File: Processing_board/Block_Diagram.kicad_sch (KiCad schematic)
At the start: 0 parts

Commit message: added Block Diagram (in KiCad and PDF) ; minor silkscreen cleanup
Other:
- note added: "16x PIN HEADER"
- note added: "1V8"
- note added: "2x PIN HEADER"
- note added: "3V3"
- note added: "4x PIN HEADER"
- note added: "5V"
- note added: "6x PIN HEADER"
- note added: "ADC"
- note added: "ADS7953"
- note added: "BGS13"
- note added: "BLE (3 DIFFERENT ANTENNA TYPES)"
- note added: "BOOT button"
- note added: "CH0 ... CH15"
- note added: "CONTROLLED IMPEDANCE 50 OHM TRACE"
- note added: "D"
- note added: "D+ D- VBUS"
- note added: "DLF162500LT"
- note added: "G"
- note added: "If PWR = 5V -> bypass 1st LDO with double jumpers PMOS blocks current from PWR when VBUS is on 5V is actually ~4.6V because of Schottky Diodes"
- note added: "LOW-PASS FILTER"
- note added: "MCP-2200"
- note added: "MCU"
- note added: "MXO AINP"
- note added: "OPA192"
- note added: "PMOS"
- note added: "POWER ADAPTATION"
- note added: "PWR"
- note added: "PWR LED"
- note added: "PWR for EMG Modules"
- note added: "REF5025"
- note added: "REFP"
- note added: "RESET button"
- note added: "RF-CAPABLE SWITCH IC"
- note added: "RX LED"
- note added: "S"
- note added: "SCK, MISO, MOSI, *CS"
- note added: "STM32WBA63CIU6"
- note added: "SWCLK SWDI SWD_TRACES NRST 3V3 GND"
- note added: "Status LED"
- note added: "TRACE ANT CHIP ANT EXTERNAL ANT"
- note added: "TX LED"
- note added: "TX RX 3V3 GND"
- note added: "TX, RX"
- note added: "USB-C CONNECTOR"
- note added: "USB-TO-UART IC"
- note added: "VBUS"
- company: N-Pulse -> (none)

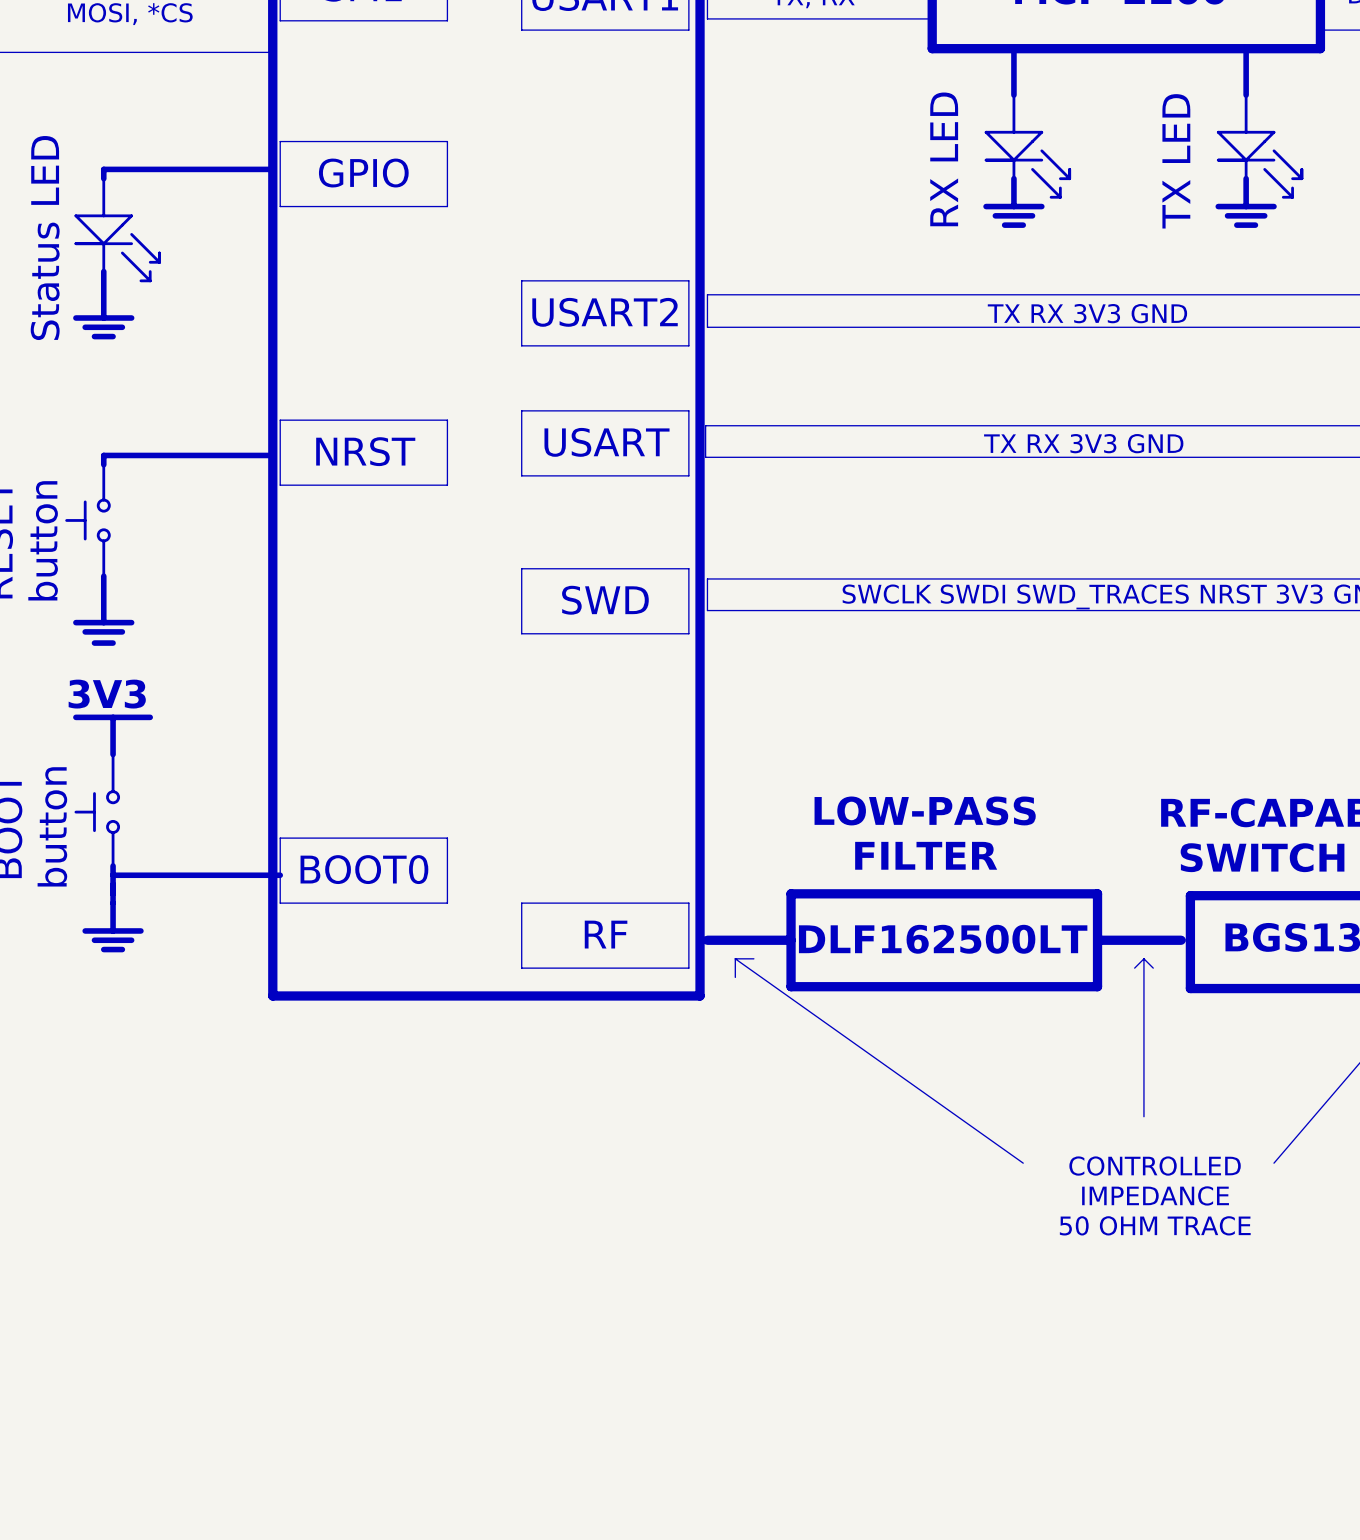
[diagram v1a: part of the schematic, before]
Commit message: UART3 doesn't exist, modified block diagram
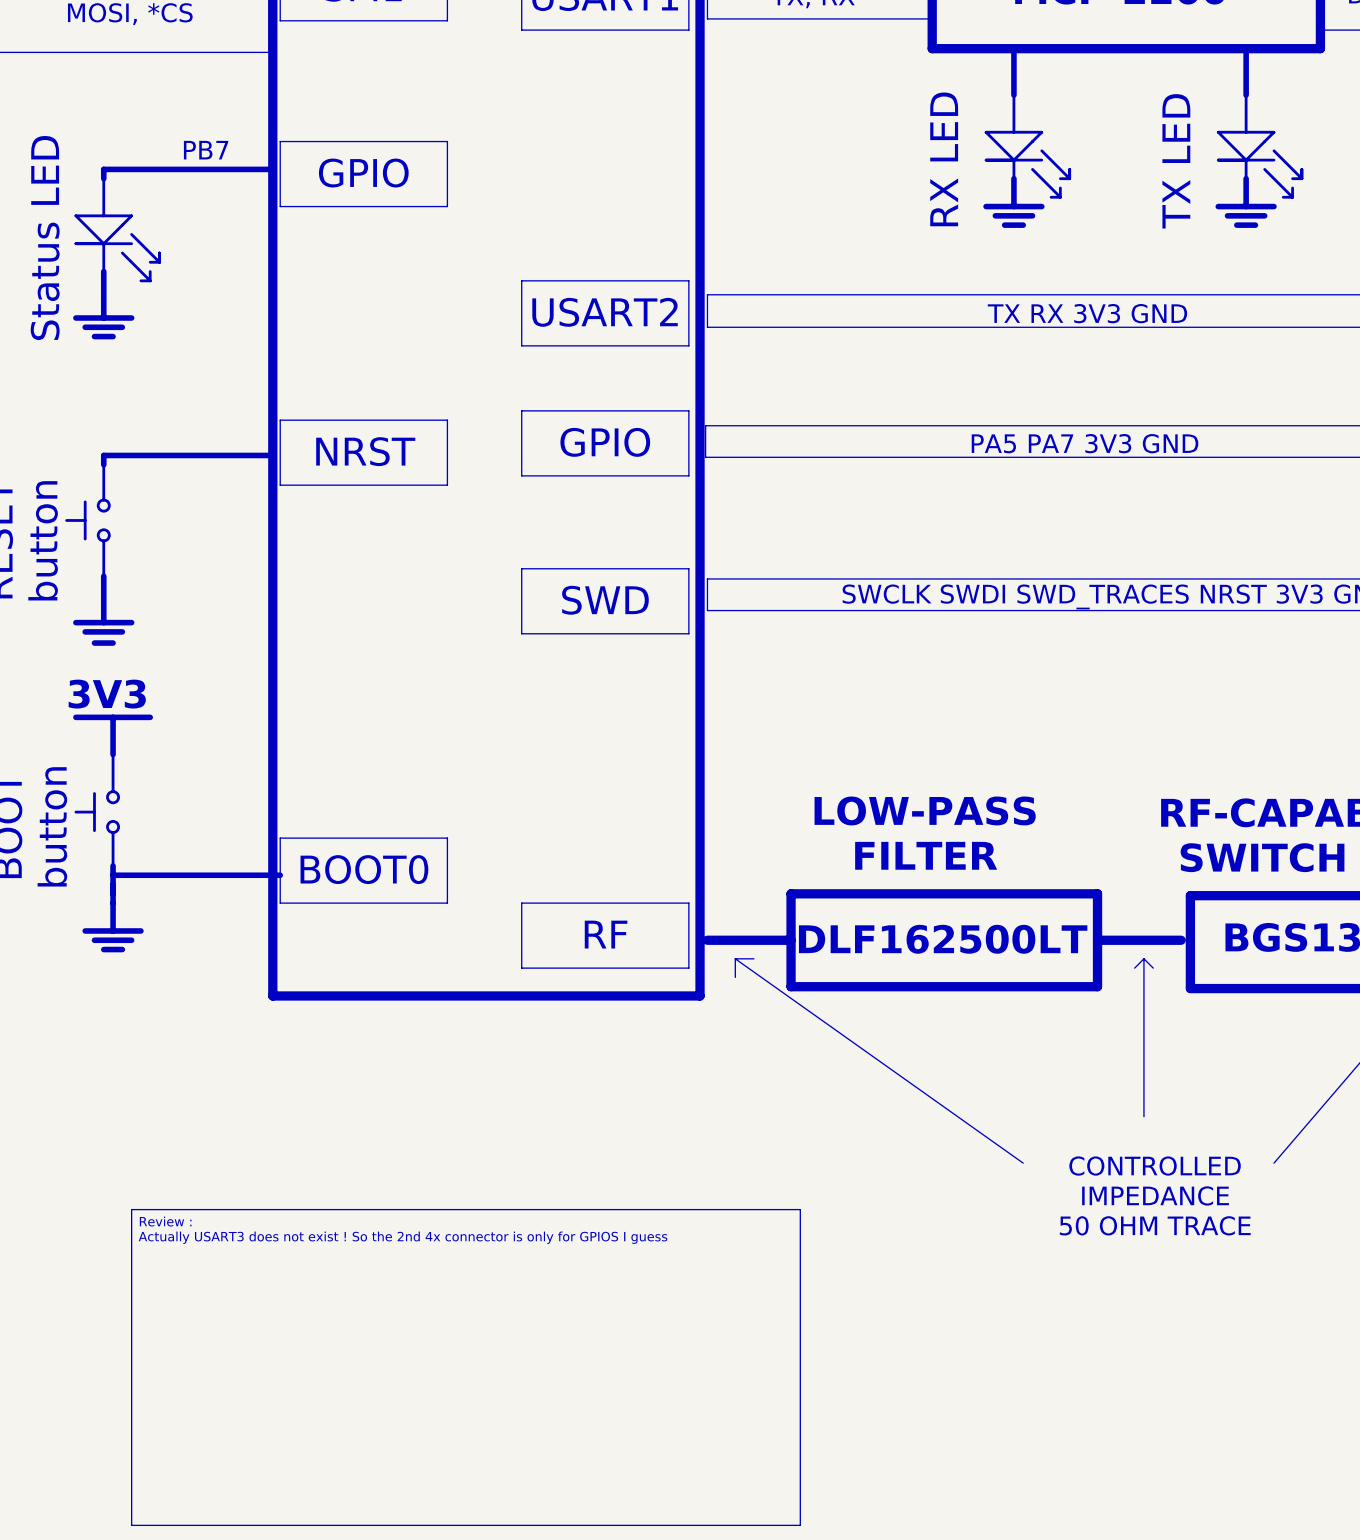
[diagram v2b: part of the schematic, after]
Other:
- note added: "PA5 PA7 3V3 GND"
- note added: "PB7"
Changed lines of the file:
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@@
 			(width 0)
 			(type solid)
-			(color 230 89 209 0.5)
-		)
-		(fill
-			(type color)
-			(color 230 89 209 0.5019607843)
+			(color 145 222 230 0.5)
+		)
+		(fill
+			(type color)
+			(color 145 222 230 0.5)
 		)
 	)
@@
 		)
 	)
-	(text "3V3"
-		(exclude_from_sim no)
-		(at 170.688 139.446 0)
-		(effects
-			(font
-				(size 3.81 3.81)
-				(thickness 0.762)
-				(bold yes)
-				(color 255 30 30 1)
-			)
-		)
-	)
-	(text "4x PIN\nHEADER"
-		(exclude_from_sim no)
-		(at 384.81 86.36 0)
-		(effects
-			(font
-				(size 3.81 3.81)
-				(thickness 0.762)
-				(bold yes)
-				(color 0 0 0 1)
-			)
-		)
-	)
-	(text "CONTROLLED \nIMPEDANCE \n50 OHM TRACE"
-		(exclude_from_sim no)
-		(at 313.944 208.026 0)
+	(text "PB7\n"
+		(exclude_from_sim no)
+		(at 184.15 65.024 0)
 		(effects
 			(font
@@
 		)
 	)
-	(text "USB-C \nCONNECTOR"
-		(exclude_from_sim no)
-		(at 385.826 44.45 0)
+	(text "3V3"
+		(exclude_from_sim no)
+		(at 170.688 139.446 0)
+		(effects
+			(font
+				(size 3.81 3.81)
+				(thickness 0.762)
+				(bold yes)
+				(color 255 30 30 1)
+			)
+		)
+	)
+	(text "4x PIN\nHEADER"
+		(exclude_from_sim no)
+		(at 384.81 86.36 0)
 		(effects
 			(font
@@
 		)
 	)
-	(text "TX RX 3V3 GND"
-		(exclude_from_sim no)
-		(at 304.292 105.156 0)
+	(text "CONTROLLED \nIMPEDANCE \n50 OHM TRACE"
+		(exclude_from_sim no)
+		(at 313.944 208.026 0)
 		(effects
 			(font
@@
 		)
 	)
+	(text "USB-C \nCONNECTOR"
+		(exclude_from_sim no)
+		(at 385.826 44.45 0)
+		(effects
+			(font
+				(size 3.81 3.81)
+				(thickness 0.762)
+				(bold yes)
+				(color 0 0 0 1)
+			)
+		)
+	)
+	(text "PA5 PA7 3V3 GND"
+		(exclude_from_sim no)
+		(at 304.292 105.156 0)
+		(effects
+			(font
+				(size 2.54 2.54)
+				(thickness 0.3175)
+				(color 0 0 0 1)
+			)
+		)
+	)
 	(text "G"
 		(exclude_from_sim no)
@@
 		)
 	)
-	(text_box "USART"
+	(text_box "NRST"
+		(exclude_from_sim no)
+		(at 194.31 101.6 0)
+		(size 22.86 8.89)
+		(margins 0.9525 0.9525 0.9525 0.9525)
+		(stroke
+			(width 0)
+			(type solid)
+		)
+		(fill
+			(type color)
+			(color 145 222 230 1)
+		)
+		(effects
+			(font
+				(size 3.81 3.81)
+				(thickness 0.4763)
+				(color 255 255 255 1)
+			)
+		)
+	)
+	(text_box "GPIO"
 		(exclude_from_sim no)
 		(at 227.33 100.33 0)
@@
 		(fill
 			(type color)
-			(color 230 89 209 1)
-		)
-		(effects
-			(font
-				(size 3.81 3.81)
-				(thickness 0.4763)
-				(color 255 255 255 1)
-			)
-		)
-	)
-	(text_box "NRST"
-		(exclude_from_sim no)
-		(at 194.31 101.6 0)
-		(size 22.86 8.89)
-		(margins 0.9525 0.9525 0.9525 0.9525)
-		(stroke
-			(width 0)
-			(type solid)
-		)
-		(fill
-			(type color)
 			(color 145 222 230 1)
 		)
@@
 		)
 	)
+	(text_box "Review :\nActually USART3 does not exist ! So the 2nd 4x connector is only for GPIOS I guess"
+		(exclude_from_sim no)
+		(at 173.99 209.55 0)
+		(size 91.44 43.18)
+		(margins 0.9525 0.9525 0.9525 0.9525)
+		(stroke
+			(width 0)
+			(type solid)
+		)
+		(fill
+			(type none)
+		)
+		(effects
+			(font
+				(size 1.27 1.27)
+			)
+			(justify left top)
+		)
+	)
